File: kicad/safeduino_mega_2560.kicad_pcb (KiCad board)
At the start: 4 copper layers, 134.5 x 63.9 mm, 130 parts, among them X1 USB

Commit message: Продолжил переделывать проект.
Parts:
- XP16, XP20, XP21, XP26, XP27, XP28, XP29, XP32, XP36, XP37, XP38, XP39, XP40, XP41, XP42, XP48, XP53, XP54, XP55, XP56, XP57, XP58, XP59, XP60, XP61, XP62, XP65, XP67, XP68, XP7: footprint 1_pin -> IWconnectors:1_pin

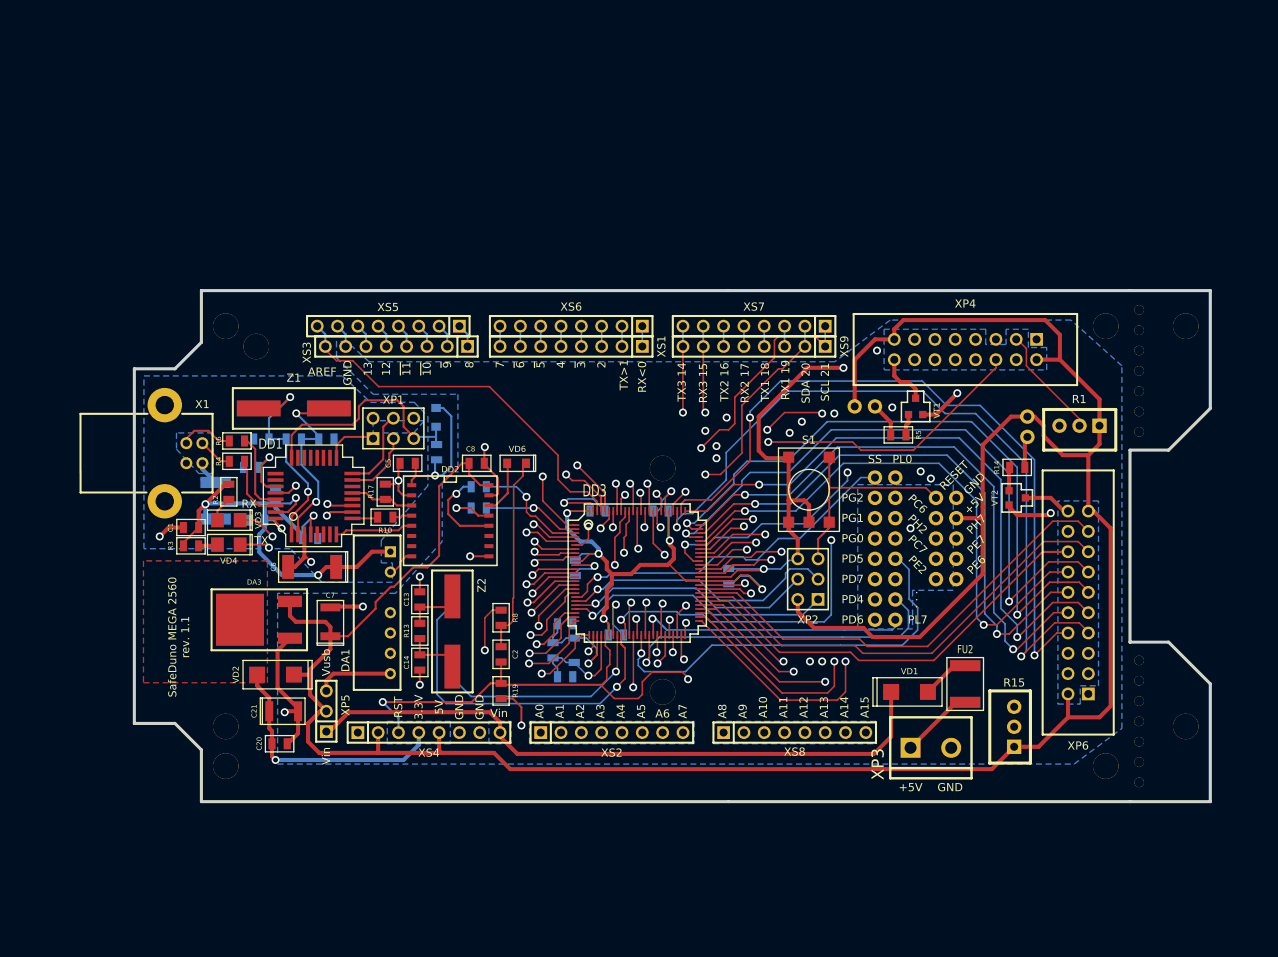
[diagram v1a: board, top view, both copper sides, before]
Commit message: Приступил к переработке платы SafeDuino MEGA 2560.
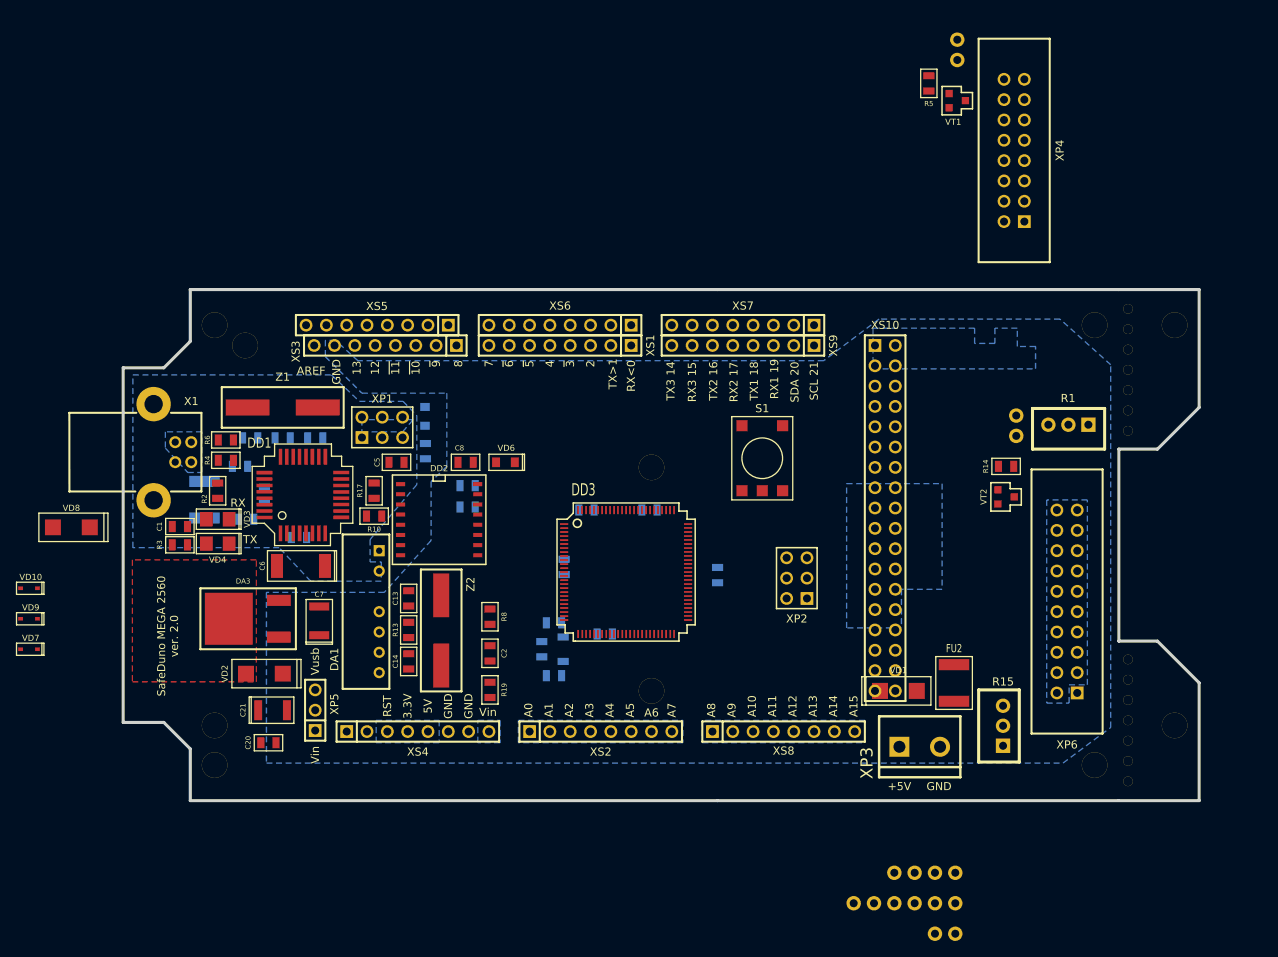
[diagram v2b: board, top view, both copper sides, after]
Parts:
- removed the ? at (179.1, 152.4)
- removed the ? at (179.1, 101.0)
- removed the ? at (179.1, 103.5)
- removed the ? at (179.1, 98.4)
- removed the ? at (179.1, 95.9)
- removed the ? at (179.1, 93.3)
- removed the ? at (179.1, 137.2)
- removed the ? at (179.1, 139.7)
- removed the ? at (179.1, 142.2)
- removed the ? at (179.1, 147.3)
- removed the ? at (179.1, 144.8)
- removed the ? at (179.1, 149.9)
- removed the ? at (179.1, 108.6)
- removed the ? at (179.1, 106.0)
- removed the G447 at (169.3, 97.8)
- removed the G447 at (170.8, 148.1)
- removed the G447 at (64.9, 149.1)
- removed the HB11460/G762 at (182.2, 147.4)
- removed the HB11460/G762 at (182.5, 95.1)
- removed XP20, XP21, XP29, XP38, XP41, XP42, XP54, XP55, XP56, XP57, XP58, XP59, XP60, XP61: ~, IWconnectors:1_pin
- removed the arduino at (69.5, 96.6)
- removed the arduino at (119.5, 139.8)
- removed the arduino at (119.5, 111.9)
- added ?: , 1_pin, F.Cu at (177.7, 152.3)
- added ?: , 1_pin, F.Cu at (177.7, 100.8)
- added ?: , 1_pin, F.Cu at (177.7, 103.4)
- added ?: , 1_pin, F.Cu at (177.7, 98.3)
- added ?: , 1_pin, F.Cu at (177.7, 95.8)
- added ?: , 1_pin, F.Cu at (177.7, 93.2)
- added ?: , 1_pin, F.Cu at (177.7, 137.0)
- added ?: , 1_pin, F.Cu at (177.7, 139.6)
- added ?: , 1_pin, F.Cu at (177.7, 142.1)
- added ?: , 1_pin, F.Cu at (177.7, 147.2)
- added ?: , 1_pin, F.Cu at (177.7, 144.7)
- added ?: , 1_pin, F.Cu at (177.7, 149.7)
- added ?: , 1_pin, F.Cu at (177.7, 108.5)
- added ?: , 1_pin, F.Cu at (177.7, 105.9)
- added G447: P***, 1_pin, F.Cu at (167.9, 97.7)
- added G447: P***, 1_pin, F.Cu at (169.4, 148.0)
- added G447: P***, 1_pin, F.Cu at (63.5, 149.0)
- added HB11460/G762: P***, 1_pin, F.Cu at (180.9, 147.3)
- added HB11460/G762: P***, 1_pin, F.Cu at (181.1, 95.0)
- added VD10: PESD5V0L1BA,115, IWcomponents:SOD323, F.Cu at (39.2, 126.9)
- added VD7: PESD5V0L1BA,115, IWcomponents:SOD323, F.Cu at (39.2, 134.5)
- added VD8: SS14, IWcomponents:SMA, F.Cu at (45.6, 119.3)
- added VD9: PESD5V0L1BA,115, IWcomponents:SOD323, F.Cu at (39.2, 130.7)
- added XS10: 2214SM-36G-75-PCP, IWconnectors:PIN_ARRAY_18x2, F.Cu at (148.6, 118.1)
- added arduino: P***, 1_pin, F.Cu at (68.1, 96.5)
- added arduino: P***, 1_pin, F.Cu at (118.1, 139.7)
- added arduino: P***, 1_pin, F.Cu at (118.1, 111.8)
- S1: value DTSGL-61K -> FSM1LP
- X1: value USB -> USBB-1J
- moved XP65 54.5 mm to (153.5, 170.1)
- moved XP7 51.9 mm to (156.1, 170.1)
- moved XP62 51.7 mm to (143.4, 166.2)
- moved XP16 50.4 mm to (156.1, 162.4)
- moved XP40 47.6 mm to (156.3, 58.3), turned to 270 degrees
- moved XP48 46.2 mm to (145.9, 166.2)
- moved XP53 46.2 mm to (148.5, 166.2)
- moved XP39 44.5 mm to (156.3, 60.8), turned to 270 degrees
- moved R5 44.1 mm to (152.8, 63.8), turned to 270 degrees
- moved XP37 43.4 mm to (151.0, 166.2)
- moved XP32 40.5 mm to (153.5, 166.2)
- moved XP36 40.5 mm to (156.1, 166.2)
- moved XP27 40.0 mm to (153.5, 162.4)
- moved VT1 38.6 mm to (156.3, 65.9), turned to 90 degrees
- moved XP26 34.5 mm to (151.0, 162.4)
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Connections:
- net Net-(R4-Pad1) renamed /UD-
- net Net-(R6-Pad1) renamed /UD+
- X1 pad 1: Net-(FU1-Pad1) -> Net-(VD7-Pad1)
- X1 pad 5: Net-(X1-Pad5) -> /GND_USB
- X1 pad 6: Net-(X1-Pad6) -> /GND_USB
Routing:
- net /MPU_VCC: track 431.2 -> 0.00 mm, vias 5 -> 0
- net /GND: track 149.2 -> 0.00 mm, vias 16 -> 0
- net /5V_USB: track 117.3 -> 0.00 mm, vias 6 -> 0
- net /RESET: track 116.1 -> 0.00 mm, vias 3 -> 0
- net /PE2: track 101.4 -> 0.00 mm, vias 1 -> 0
- net /PA0: track 94.1 -> 0.00 mm, vias 2 -> 0
- net /PE6: track 93.9 -> 0.00 mm, vias 1 -> 0
- net /PA1: track 89.0 -> 0.00 mm, vias 2 -> 0
- net /PE7: track 88.7 -> 0.00 mm, vias 1 -> 0
- net /PH2: track 83.7 -> 0.00 mm, vias 3 -> 0
- net /VCCIN: track 82.4 -> 0.00 mm
- net /PH7: track 81.2 -> 0.00 mm, vias 1 -> 0
- net /PA4: track 81.1 -> 0.00 mm, vias 2 -> 0
- net /PL1: track 81.0 -> 0.00 mm, vias 1 -> 0
- net /PA6: track 78.7 -> 0.00 mm, vias 2 -> 0
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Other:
- net class Default: clearance 0.254 -> 0.25; trace_width 0.254 -> 0.2; via_dia 1.19888 -> 1; via_drill 0.59944 -> 0.6
- rule pad_to_mask_clearance: 0.254 -> 0.25
- rule trace_clearance: 0.254 -> 0.25
- rule trace_min: 0.20066 -> 0.2
- rule via_min_drill: 0.508 -> 0.5
- rule via_min_size: 0.889 -> 0.8
- board text added: "SafeDuno MEGA 2560 ver. 2.0"
- board text removed: ". . ."
- board text removed: "PC6"
- board text removed: "PC7"
- board text removed: "PD4"
- board text removed: "PD5"
- board text removed: "PD6"
- board text removed: "PD7"
- board text removed: "PE2"
- board text removed: "PE6"
- board text removed: "PE7"
- board text removed: "PG0"
- board text removed: "PG1"
- board text removed: "PG2"
- board text removed: "PH2"
- board text removed: "PH7"
- board text removed: "PL0"
- board text removed: "PL7"
- board text removed: "RESET"
- board text removed: "SS"
- board text removed: "SafeDuno MEGA 2560 rev. 1.1"

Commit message: Продолжил переделывать SafeDuino MEGA 2560.
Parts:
- removed XP16, XP26, XP27, XP28, XP32, XP36, XP37, XP39, XP40, XP48, XP53, XP62, XP65, XP67, XP68: ~, IWconnectors:1_pin
- added LL1: MMZ2012R601AT000, IWsmd_case:SMD0805, F.Cu at (78.0, 125.0)
- added XP8: PLS-2, IWconnectors:PIN_ARRAY_2x1, F.Cu at (162.6, 106.9)
- added XS11: PBS-10, IWconnectors:PIN_ARRAY_10x1, F.Cu at (142.2, 71.1)
- added arduino: P***, 1_pin, F.Cu at (142.2, 96.5)
- added arduino: P***, 1_pin, F.Cu at (147.6, 144.8)
- C13, C14, C15, C16, C17, C18, C19, C2, C20, C22, C23, C3, C4, C8, R10, R11, R12, R13, R14, R17, R18, R19, R2, R3, R4, R5, R6, R7, R8, R9: footprint IWsmd_case:SMD0805 -> IWsmd_case:SMD0603
- C6: value 100мк 10В -> 4.7 мк 50В
- DA1: value P10LU-0505ELF -> SPU03L-05
- VD10, VD7, VD9: moved to B.Cu
- XP7: value ~ -> PLS-2; footprint IWconnectors:1_pin -> IWconnectors:PIN_ARRAY_2x1
- moved XP7 111.1 mm to (155.4, 58.9)
- moved VD7 28.5 mm to (56.4, 111.8), turned to 180 degrees
- moved VD9 28.3 mm to (56.4, 108.2), turned to 180 degrees
- moved VD10 24.1 mm to (56.4, 110.0), turned to 180 degrees
- moved R15 16.0 mm to (162.6, 130.6)
- moved FU2 6.10 mm to (162.0, 138.7)
- moved VD1 6.10 mm to (155.1, 139.7)
- moved XP3 6.10 mm to (157.7, 146.7)
- moved C6 2.16 mm to (72.1, 124.1)
- moved S1 1.66 mm to (131.8, 112.0)
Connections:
- net /UD+ renamed /USB_D+
- net /UD- renamed /USB_D-
- DA1 pad 1: /5V_USB -> Net-(DA1-Pad1)
- FU1 pad 2: /5V_USB -> Net-(FU1-Pad2)
- VD7 pad 1: Net-(VD7-Pad1) -> Net-(FU1-Pad1)
- VD8 pad 1: Net-(VD7-Pad1) -> Net-(FU1-Pad2)
- VD8 pad 2: Net-(FU1-Pad1) -> /5V_USB
- X1 pad 1: Net-(VD7-Pad1) -> Net-(FU1-Pad1)
- XP7 pad 1: /MPU_VCC -> Net-(R5-Pad1)
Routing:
- net /USB_D-: track 0.00 -> 12.4 mm
- net /D-: track 0.00 -> 9.59 mm
- net /D+: track 0.00 -> 9.59 mm
- net /USB_D+: track 0.00 -> 9.34 mm
- net Net-(FU1-Pad1): track 0.00 -> 6.20 mm, vias 0 -> 1

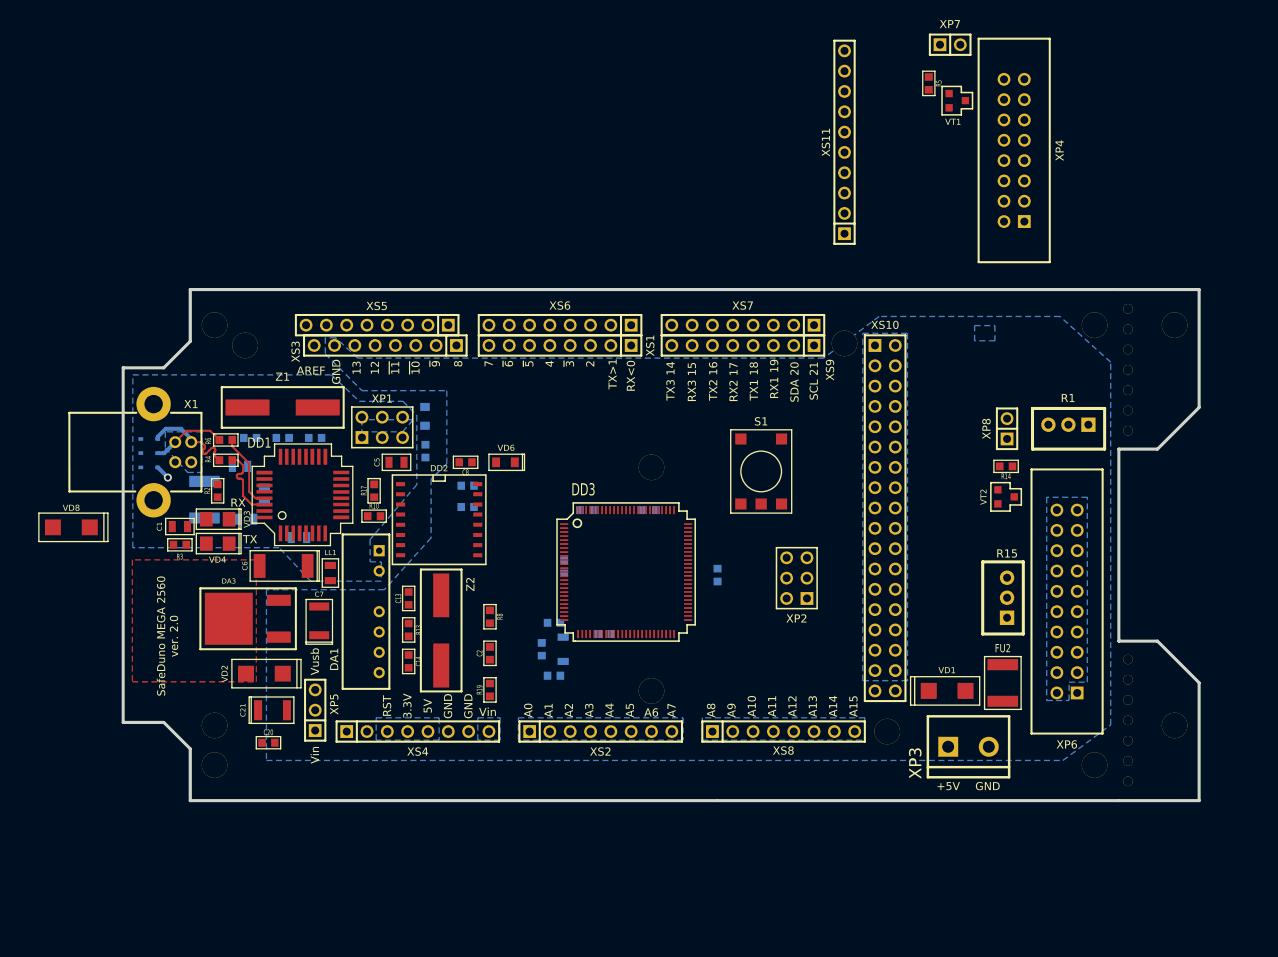
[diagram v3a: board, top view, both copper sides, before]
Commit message: Продолжил переделывать печатную плату SafeDuino MEGA 2560.
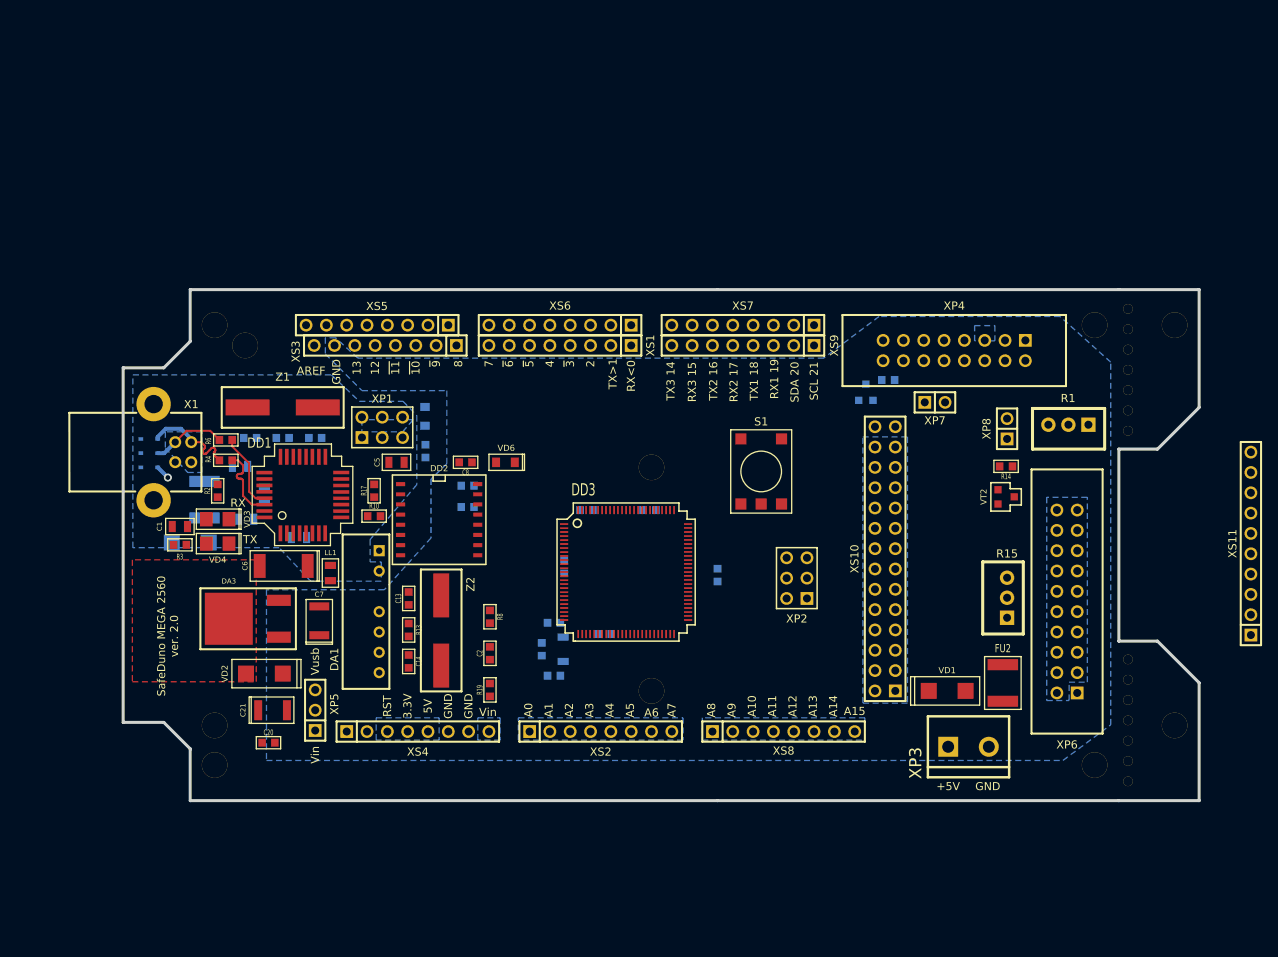
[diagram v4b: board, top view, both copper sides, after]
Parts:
- removed the arduino at (142.2, 96.5)
- removed the arduino at (147.6, 144.8)
- R5, VD8, VT1: moved to B.Cu
- XS10: value 2214SM-36G-75-PCP -> PBD-28; footprint IWconnectors:PIN_ARRAY_18x2 -> IWconnectors:PIN_ARRAY_14x2
- moved XS11 71.4 mm to (193.0, 121.3)
- moved XP7 44.7 mm to (153.5, 103.6)
- moved VT1 38.2 mm to (144.9, 102.4), turned to 0 degrees
- moved R5 37.4 mm to (147.7, 100.8), turned to 180 degrees
- moved XP4 26.1 mm to (156.0, 97.2), turned to 180 degrees
- moved VD8 15.0 mm to (60.5, 121.2), turned to 180 degrees
- moved XS10 5.68 mm to (146.1, 123.2), turned to 90 degrees
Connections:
- XS10 pad 27: /PA7 -> /GND
- XS10 pad 28: /PA6 -> /GND
- XS10 pad 3: /PB0 -> /SS
- XS10 pad 4: /PB1 -> /SCK
- XS10 pad 5: /PB2 -> /MOSI
- XS10 pad 6: /PB3 -> /MISO
